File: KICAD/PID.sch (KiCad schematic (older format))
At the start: 4 parts, among them U3 Opamp_Dual_Generic

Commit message: removed legacy symbols
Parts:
- removed JP4, JP5: Jumper_NC_Small, symbol sesame-fonctionnel-rescue:Jumper_NC_Small-device
- removed U3: Opamp_Dual_Generic, symbol sesame-fonctionnel-rescue:Opamp_Dual_Generic-device
- added JP? (x2): Jumper_NO_Small, symbol Device:Jumper_NO_Small
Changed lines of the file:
@@
 $Descr A4 11693 8268
 encoding utf-8
-Sheet 12 15
+Sheet 10 15
 Title "SESAME"
 Date ""
@@
 Comment4 ""
 $EndDescr
-Text HLabel 3150 3150 0    50   Input ~ 0
+Text HLabel 3150 3250 0    50   Input ~ 0
 Selected_Measure
-Text Label 3300 3150 0    50   ~ 0
+Text Label 3300 3250 0    50   ~ 0
 Sel_Measure_In
-Text Label 4550 3150 0    50   ~ 0
+Text Label 4550 3250 0    50   ~ 0
 Sel_Measure_Ext
 Wire Wire Line
-	3150 3150 3900 3150
+	3150 3250 3900 3250
 Text HLabel 3150 2950 0    50   Input ~ 0
 Ext_Consign
@@
 Text Label 1200 1150 0    50   ~ 0
 Consign_Ext
-$Comp
-L sesame-fonctionnel-rescue:Jumper_NC_Small-device JP4
-U 1 1 61D0773B
-P 4000 2950
-AR Path="/61D0773B" Ref="JP4"  Part="1"
-AR Path="/60F1B237/61D0773B" Ref="JP4"  Part="1"
-F 0 "JP4" H 4000 3150 50  0000 C CNN
-F 1 "Jumper_NC_Small" H 4000 3071 50  0000 C CNN
-F 2 "" H 4000 2950 50  0001 C CNN
-F 3 "~" H 4000 2950 50  0001 C CNN
-	1    4000 2950
-	1    0    0    -1
-$EndComp
 Wire Wire Line
 	3150 2950 3900 2950
-$Comp
-L sesame-fonctionnel-rescue:Jumper_NC_Small-device JP5
-U 1 1 61D09C0A
-P 4000 3150
-AR Path="/61D09C0A" Ref="JP5"  Part="1"
-AR Path="/60F1B237/61D09C0A" Ref="JP5"  Part="1"
-F 0 "JP5" H 4000 2950 50  0000 C CNN
-F 1 "Jumper_NC_Small" H 4000 3050 50  0000 C CNN
-F 2 "" H 4000 3150 50  0001 C CNN
-F 3 "~" H 4000 3150 50  0001 C CNN
-	1    4000 3150
-	1    0    0    -1
-$EndComp
 Wire Wire Line
 	4100 2950 5250 2950
 Wire Wire Line
-	4100 3150 5250 3150
-$Comp
-L sesame-fonctionnel-rescue:Opamp_Dual_Generic-device U3
-U 1 1 61B777D2
-P 5550 3050
-AR Path="/61B777D2" Ref="U3"  Part="1"
-AR Path="/60F1B237/61B777D2" Ref="U3"  Part="1"
-F 0 "U3" H 5550 3417 50  0000 C CNN
-F 1 "Opamp_Dual_Generic" H 5550 3326 50  0000 C CNN
-F 2 "" H 5550 3050 50  0001 C CNN
-F 3 "~" H 5550 3050 50  0001 C CNN
-	1    5550 3050
-	1    0    0    -1
-$EndComp
+	4100 3250 5250 3250
 Wire Notes Line
 	600  2150 600  550
@@
 Wire Wire Line
 	1200 1250 1100 1250
+$Comp
+L Device:Jumper_NO_Small JP?
+U 1 1 610BA839
+P 4000 2950
+F 0 "JP?" H 4000 3135 50  0000 C CNN
+F 1 "Jumper_NO_Small" H 4000 3044 50  0000 C CNN
+F 2 "" H 4000 2950 50  0001 C CNN
+F 3 "~" H 4000 2950 50  0001 C CNN
+	1    4000 2950
+	1    0    0    -1
+$EndComp
+$Comp
+L Device:Jumper_NO_Small JP?
+U 1 1 610BB003
+P 4000 3250
+F 0 "JP?" H 4000 3435 50  0000 C CNN
+F 1 "Jumper_NO_Small" H 4000 3344 50  0000 C CNN
+F 2 "" H 4000 3250 50  0001 C CNN
+F 3 "~" H 4000 3250 50  0001 C CNN
+	1    4000 3250
+	1    0    0    -1
+$EndComp
 $EndSCHEMATC

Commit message: labels dans les blocks
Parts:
- removed JP? (x2): Jumper_NO_Small, symbol Device:Jumper_NO_Small
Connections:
- net labels added: Feedback, Measure_Selected
- net labels removed: Selected_Measure
- wire segments 16 -> 12
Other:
- note added: "Entrées"
- note added: "Sortie"
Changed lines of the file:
@@
 $Descr A4 11693 8268
 encoding utf-8
-Sheet 10 15
+Sheet 9 15
 Title "SESAME"
 Date ""
@@
 Comment4 ""
 $EndDescr
-Text HLabel 3150 3250 0    50   Input ~ 0
-Selected_Measure
-Text Label 3300 3250 0    50   ~ 0
-Sel_Measure_In
-Text Label 4550 3250 0    50   ~ 0
-Sel_Measure_Ext
-Wire Wire Line
-	3150 3250 3900 3250
-Text HLabel 3150 2950 0    50   Input ~ 0
+Text HLabel 5300 3550 0    50   Input ~ 0
+Measure_Selected
+Text HLabel 5300 3400 0    50   Input ~ 0
 Ext_Consign
-Text Label 3350 2950 0    50   ~ 0
-Consign_In
-Text Label 4550 2950 0    50   ~ 0
-Consign_Ext
 $Comp
 L Sesame:SESAME_SHIELD SLD1
@@
 Text Label 1200 1150 0    50   ~ 0
 Consign_Ext
-Wire Wire Line
-	3150 2950 3900 2950
-Wire Wire Line
-	4100 2950 5250 2950
-Wire Wire Line
-	4100 3250 5250 3250
 Wire Notes Line
 	600  2150 600  550
@@
 Wire Wire Line
 	1200 1250 1100 1250
-$Comp
-L Device:Jumper_NO_Small JP?
-U 1 1 610BA839
-P 4000 2950
-F 0 "JP?" H 4000 3135 50  0000 C CNN
-F 1 "Jumper_NO_Small" H 4000 3044 50  0000 C CNN
-F 2 "" H 4000 2950 50  0001 C CNN
-F 3 "~" H 4000 2950 50  0001 C CNN
-	1    4000 2950
-	1    0    0    -1
-$EndComp
-$Comp
-L Device:Jumper_NO_Small JP?
-U 1 1 610BB003
-P 4000 3250
-F 0 "JP?" H 4000 3435 50  0000 C CNN
-F 1 "Jumper_NO_Small" H 4000 3344 50  0000 C CNN
-F 2 "" H 4000 3250 50  0001 C CNN
-F 3 "~" H 4000 3250 50  0001 C CNN
-	1    4000 3250
-	1    0    0    -1
-$EndComp
+Text HLabel 5850 3450 2    50   Output ~ 0
+Feedback
+Text Notes 4850 3750 0    50   ~ 0
+Entrées
+Text Notes 5950 3650 0    50   ~ 0
+Sortie
+Wire Notes Line
+	6300 3350 6300 3700
+Wire Notes Line
+	6300 3700 5800 3700
+Wire Notes Line
+	5800 3700 5800 3350
+Wire Notes Line
+	5800 3350 6300 3350
+Wire Notes Line
+	5400 3300 4500 3300
+Wire Notes Line
+	4500 3300 4500 3800
+Wire Notes Line
+	4500 3800 5400 3800
+Wire Notes Line
+	5400 3800 5400 3300
 $EndSCHEMATC

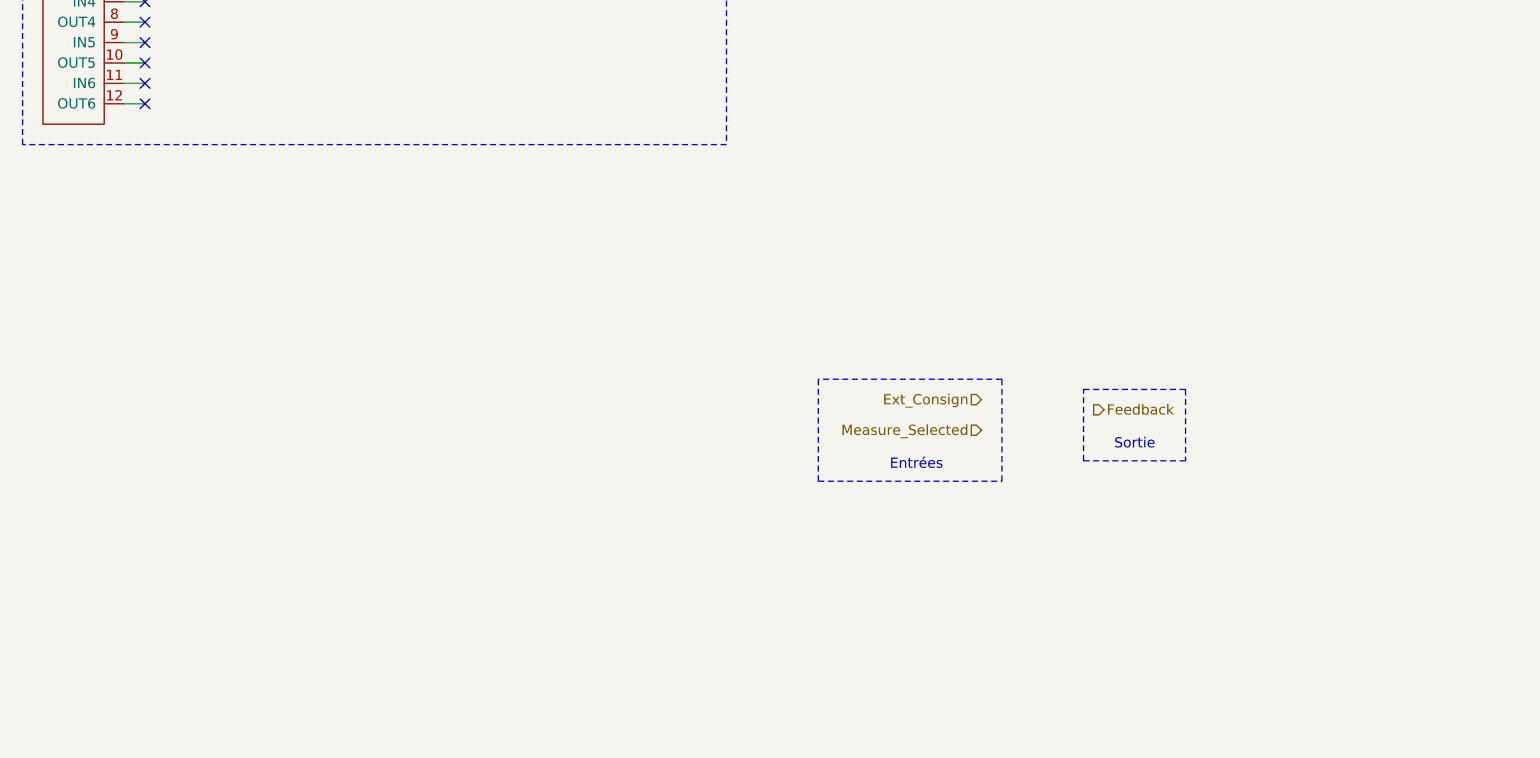
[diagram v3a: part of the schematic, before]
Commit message: added draft pwm gen & pid
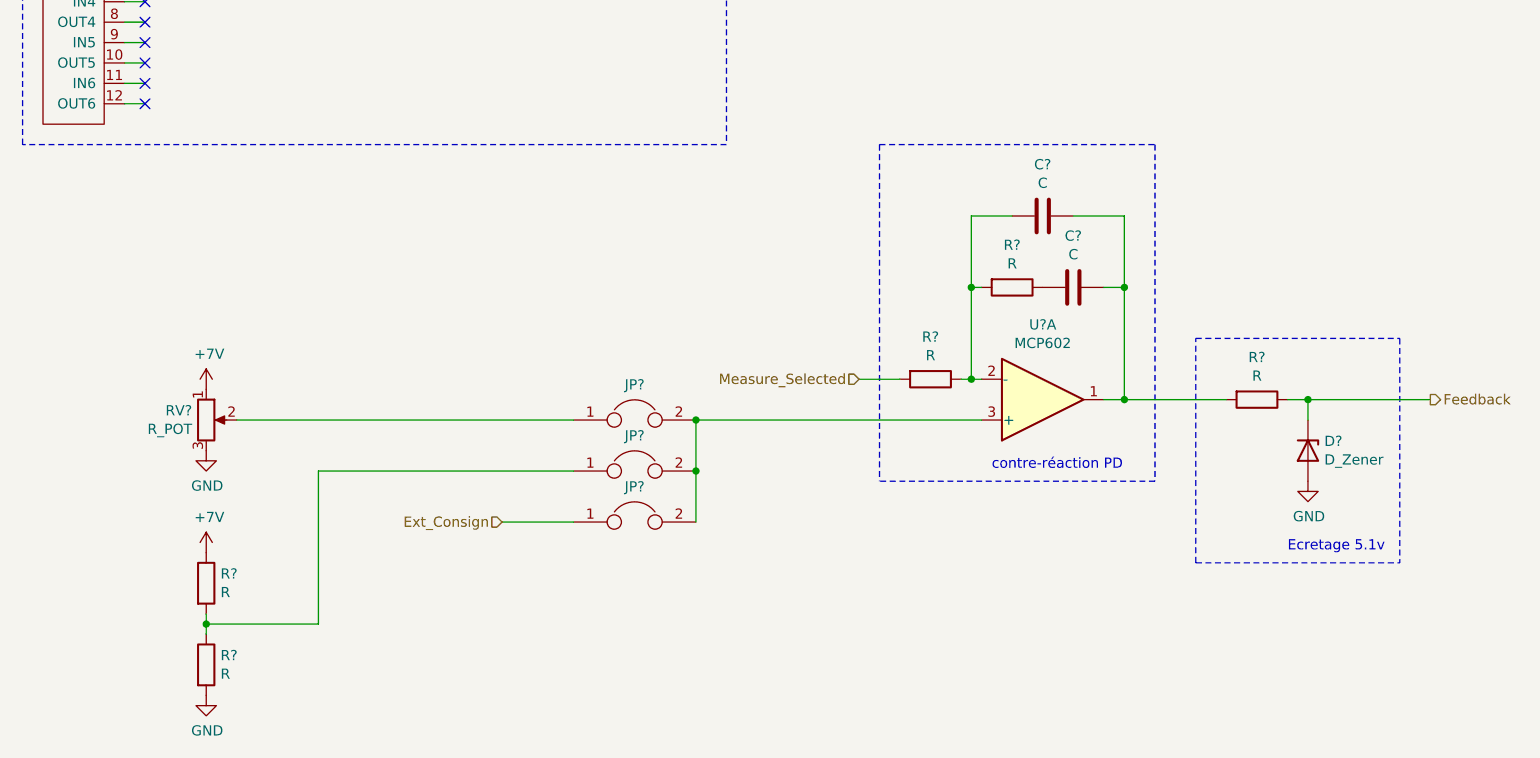
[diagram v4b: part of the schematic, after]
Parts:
- added C? (x2): C, symbol Device:C
- added D?: D_Zener, symbol Device:D_Zener
- added JP? (x3): Jumper, symbol Device:Jumper
- added R? (x5): R, symbol Device:R
- added RV?: R_POT, symbol Device:R_POT
- added U?: MCP602, symbol Amplifier_Operational:MCP602
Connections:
- net Ext_Consign: now also JP?.1
- net Feedback: now also D?.1 (K), R?.1
- net Measure_Selected: now also R?.2
- new net: C?.1, C?.1, R?.2, U?.1
- new net: C?.2, R?.1, R?.2, U?.2 (-)
- new net: JP?.2, JP?.2, JP?.2, U?.3 (+)
- new net: JP?.1, R?.1, R?.2
- new net: JP?.1, RV?.2
- new net: C?.2, R?.1
- new net +7V: R?.1, RV?.1
- new net GND: D?.2 (A), R?.2, RV?.3
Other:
- note added: "Ecretage 5.1v"
- note added: "contre-réaction PD"
- note removed: "Entrées"
- note removed: "Sortie"

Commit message: a ton of new stuff. V0.8
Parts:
- removed R? (x2): R, symbol Device:R
- removed RV?: R_POT, symbol Device:R_POT
- added C? (x2): C, symbol Device:C
- added C?: 100n, symbol Device:C
- added R? (x6): R, symbol Device:R
- added RV?: R_POT, symbol Device:R_POT
- added U?: LM7332, symbol Amplifier_Operational:LM7332
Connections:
- net Ext_Consign: now also R?.2; no longer JP?.1
- net GND: now also C?.2, C?.2, R?.2, RV?.3, U?.8 (V+)
- net Measure_Selected: now also R?.2
- net at C?.2, R?.1, R?.2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: now also C?.1
- net at JP?.2, JP?.2, JP?.2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: now also C?.1
- net at JP?.1: now also R?.1 (x2)
- new net: C?.2, R?.1
- new net: JP?.1, R?.1
- new net: R?.2, RV?.2
- new net: R?.1, R?.2, R?.2
- new net VCC: C?.1, U?.4 (V-)
- new net VREF: R?.1, RV?.1
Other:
- note added: "Alim. AOP"
- note added: "Consigne Fixe\nInterne"
- note added: "Consigne Potentiometre\nInterne"
- note added: "Soft start\nenv 1ms\nDemare apres le Enable (du driver)"
- note added: "contre-réaction PID"
- note removed: "contre-réaction PD"
- moved on the sheet: C?, D?, JP?, R?, U?A

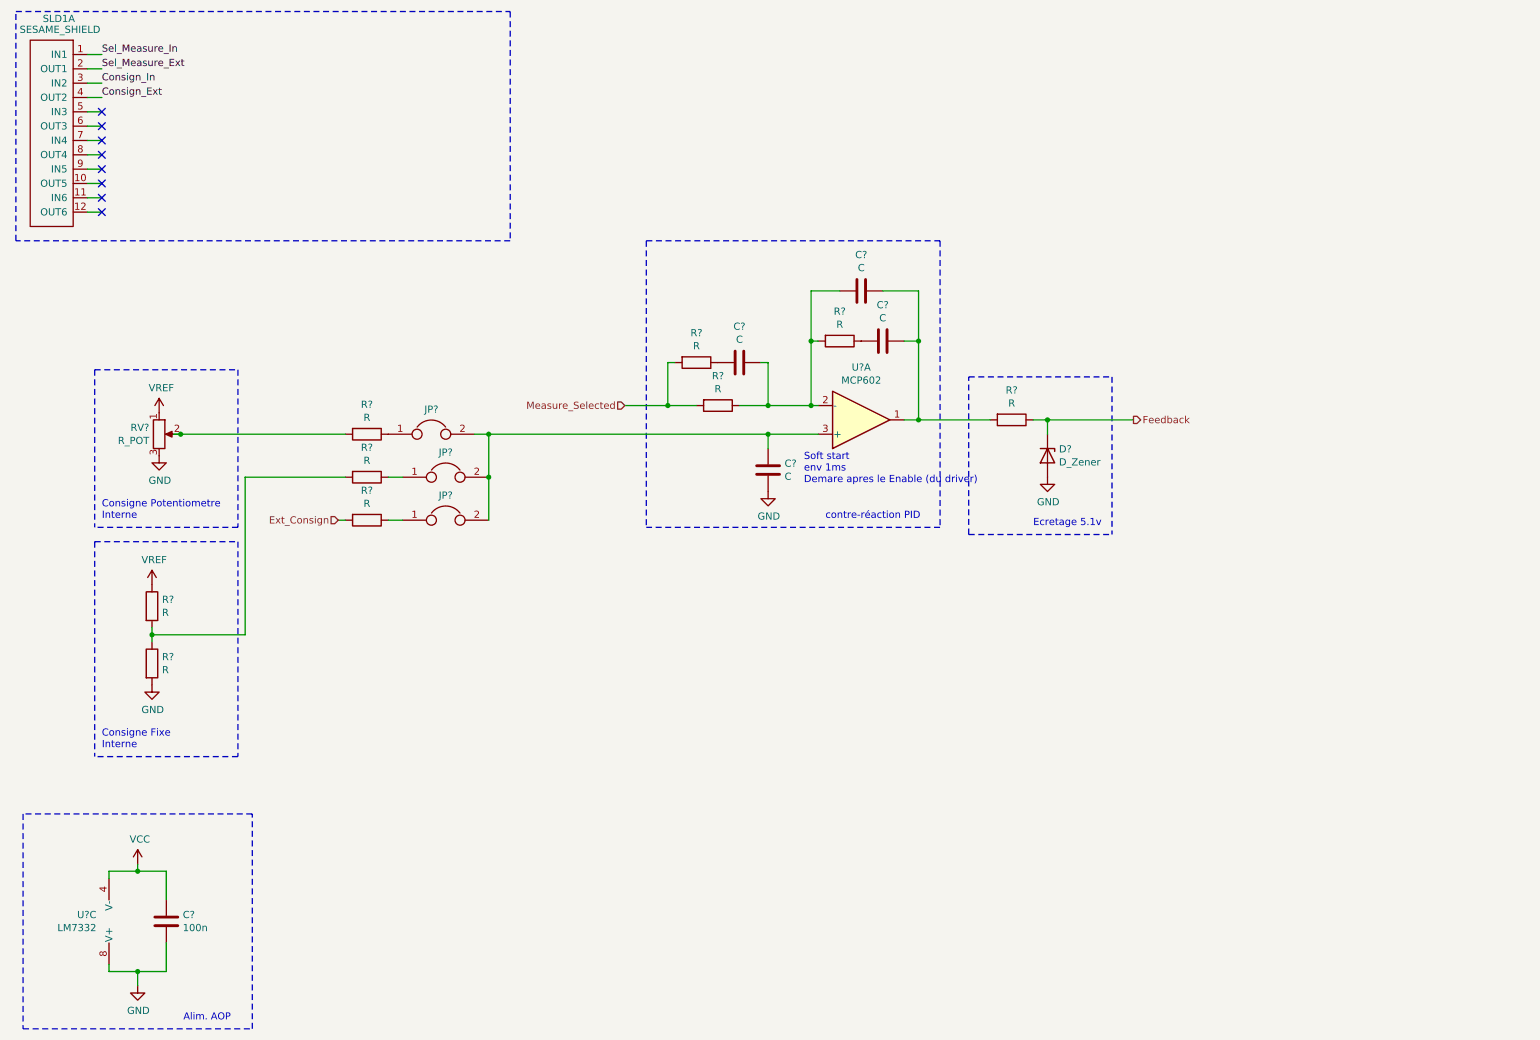
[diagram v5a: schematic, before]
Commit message: PID + PWM + RAMP finished
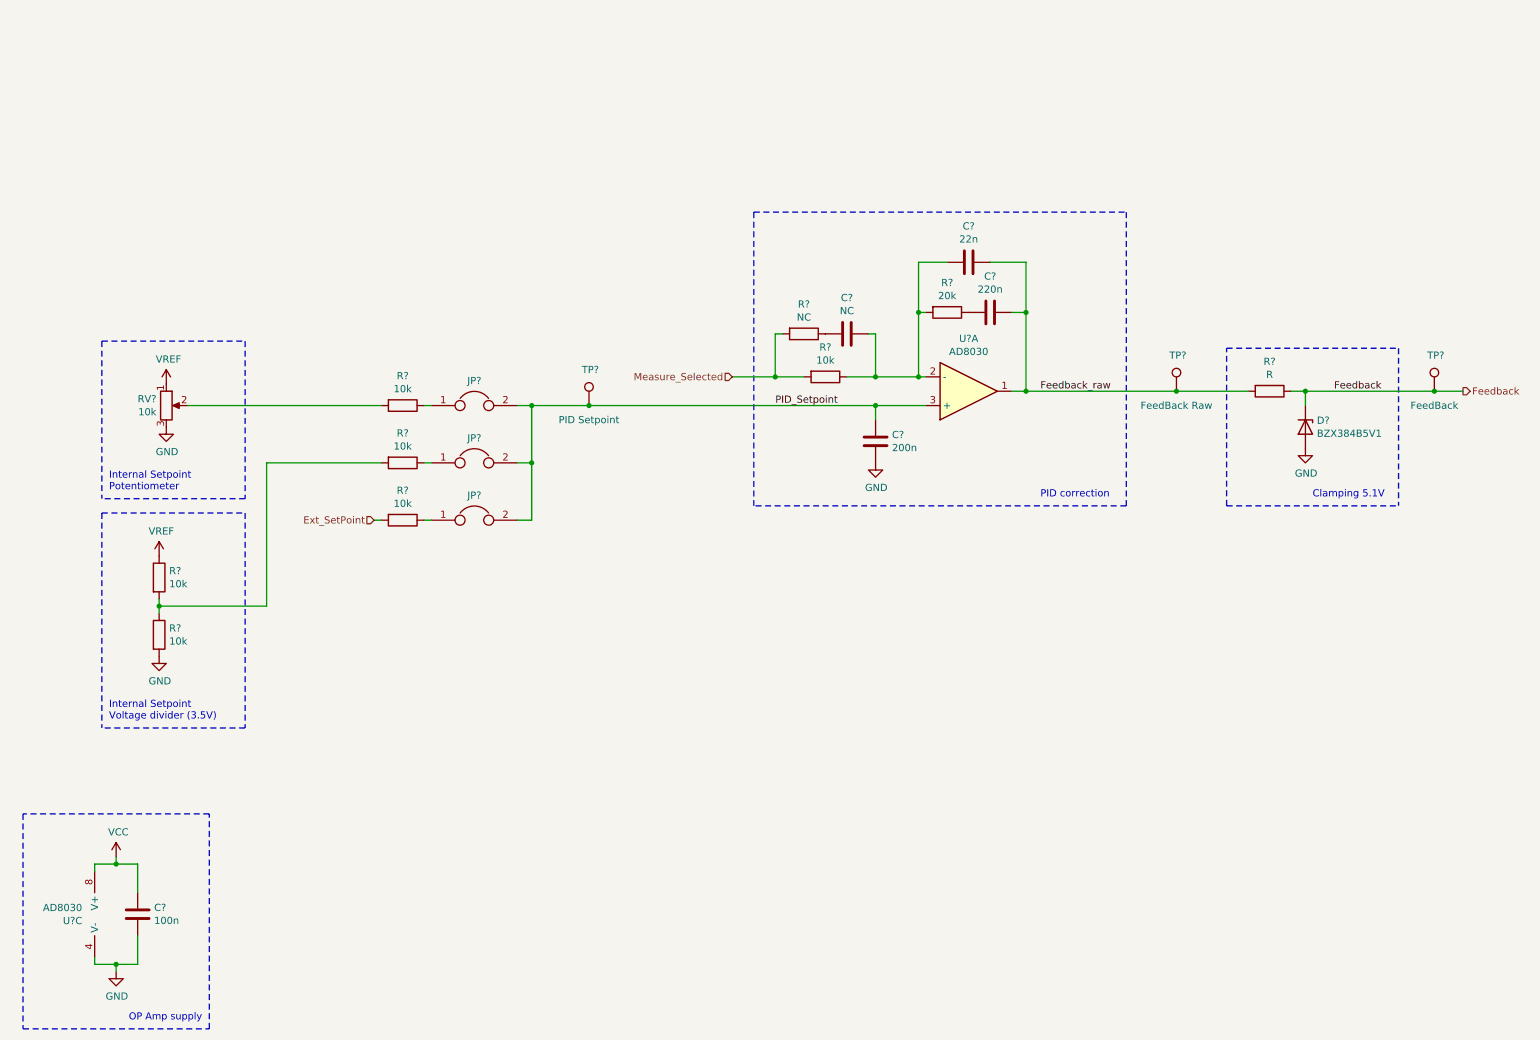
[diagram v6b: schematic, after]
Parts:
- removed C?: 100n, symbol Device:C
- removed JP?: Jumper, symbol Device:Jumper
- removed SLD1: SESAME_SHIELD, symbol Sesame:SESAME_SHIELD
- removed U?: LM7332, symbol Amplifier_Operational:LM7332
- removed U?: MCP602, symbol Amplifier_Operational:MCP602
- added C?: 100n, Capacitor_SMD:C_0805_2012Metric_Pad1.15x1.40mm_HandSolder, symbol Device:C
- added JP?: Jumper, symbol Device:Jumper
- added TP?: FeedBack Raw, symbol Connector:TestPoint
- added TP?: FeedBack, symbol Connector:TestPoint
- added TP?: PID Setpoint, symbol Connector:TestPoint
- added U? (x2): AD8030, symbol Sesame:AD8030
- C?: value C -> NC; footprint (none) -> Capacitor_SMD:C_0805_2012Metric_Pad1.15x1.40mm_HandSolder
- C?: value C -> 200n; footprint (none) -> Capacitor_SMD:C_0805_2012Metric_Pad1.15x1.40mm_HandSolder
- C?: value C -> 22n; footprint (none) -> Capacitor_SMD:C_0805_2012Metric_Pad1.15x1.40mm_HandSolder
- C?: value C -> 220n; footprint (none) -> Capacitor_SMD:C_0805_2012Metric_Pad1.15x1.40mm_HandSolder
- D?: value D_Zener -> BZX384B5V1; footprint (none) -> Diode_SMD:D_SOD-323_HandSoldering
- R?: value R -> NC; footprint (none) -> Resistor_SMD:R_0805_2012Metric_Pad1.15x1.40mm_HandSolder
- R? (x6): value R -> 10k; footprint (none) -> Resistor_SMD:R_0805_2012Metric_Pad1.15x1.40mm_HandSolder
- R?: value R -> 20k; footprint (none) -> Resistor_SMD:R_0805_2012Metric_Pad1.15x1.40mm_HandSolder
- R?: footprint (none) -> Resistor_SMD:R_0805_2012Metric_Pad1.15x1.40mm_HandSolder
- RV?: value R_POT -> 10k
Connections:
- net Feedback: now also TP?.1
- net GND: now also C?.2, U?.4 (V-)
- net VCC: now also C?.1, U?.8 (V+)
- net at C?.1, C?.2, R?.1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: now also U?.2 (-)
- net PID_Setpoint: now reaches C?.1, JP?.2, JP?.2
- net PID_Setpoint: now also JP?.2, TP?.1, U?.3 (+)
- net at R?.1: now also JP?.1
- net Feedback_raw: now reaches C?.1, C?.1, R?.2
- net Feedback_raw: now also TP?.1, U?.1
- net Ext_Consign renamed Ext_SetPoint
- no-connect marks 8 -> 0
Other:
- note added: "Clamping 5.1V"
- note added: "Internal Setpoint\nPotentiometer"
- note added: "Internal Setpoint\nVoltage divider (3.5V)"
- note added: "OP Amp supply"
- note added: "PID correction"
- note removed: "Alim. AOP"
- note removed: "Consigne Fixe\nInterne"
- note removed: "Consigne Potentiometre\nInterne"
- note removed: "Ecretage 5.1v"
- note removed: "Soft start\nenv 1ms\nDemare apres le Enable (du driver)"
- note removed: "contre-réaction PID"
- moved on the sheet: C?, D?, JP?, R?, RV?

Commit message: mainly footprints
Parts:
- U1: renamed from U?; footprint (none) -> Package_SO:SO-8_3.9x4.9mm_P1.27mm
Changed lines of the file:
@@
 $Descr A4 11693 8268
 encoding utf-8
-Sheet 8 16
+Sheet 4 16
 Title "SESAME"
 Date ""
@@
 P 1250 6850
 AR Path="/60F1AF26/6124BDFD" Ref="U?"  Part="3"
-AR Path="/60F1B237/6124BDFD" Ref="U?"  Part="3"
-F 0 "U?" H 1063 6804 50  0000 R CNN
+AR Path="/60F1B237/6124BDFD" Ref="U1"  Part="3"
+F 0 "U1" H 1063 6804 50  0000 R CNN
 F 1 "AD8030" H 1063 6895 50  0000 R CNN
-F 2 "" H 1250 6850 50  0001 C CNN
+F 2 "Package_SO:SO-8_3.9x4.9mm_P1.27mm" H 1250 6850 50  0001 C CNN
 F 3 "~" H 1250 6850 50  0001 C CNN
 	3    1250 6850
@@
 $EndComp
 $Comp
-L Sesame:AD8030 U?
+L Sesame:AD8030 U1
 U 1 1 6125EDE1
 P 7250 3200
-F 0 "U?" H 7250 2833 50  0000 C CNN
+F 0 "U1" H 7250 2833 50  0000 C CNN
 F 1 "AD8030" H 7250 2924 50  0000 C CNN
-F 2 "" H 7250 3200 50  0001 C CNN
+F 2 "Package_SO:SO-8_3.9x4.9mm_P1.27mm" H 7250 3200 50  0001 C CNN
 F 3 "~" H 7250 3200 50  0001 C CNN
 	1    7250 3200

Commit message: revex with jmt
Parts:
- TP?: value FeedBack Raw -> TP_NOP
- TP?: value FeedBack -> TP_POP
- TP?: value PID Setpoint -> TP_POP
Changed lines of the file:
@@
 $Descr A4 11693 8268
 encoding utf-8
-Sheet 4 16
+Sheet 3 16
 Title "SESAME"
 Date ""
@@
 AR Path="/60F1B237/612E229E" Ref="TP?"  Part="1"
 F 0 "TP?" H 8650 3450 50  0000 L CNN
-F 1 "FeedBack Raw" H 8700 3100 50  0000 C CNN
+F 1 "TP_NOP" H 8700 3100 50  0000 C CNN
 F 2 "" H 8900 3200 50  0001 C CNN
 F 3 "~" H 8900 3200 50  0001 C CNN
@@
 AR Path="/60F1B237/612E6FF3" Ref="TP?"  Part="1"
 F 0 "TP?" H 10450 3450 50  0000 L CNN
-F 1 "FeedBack" H 10500 3100 50  0000 C CNN
+F 1 "TP_POP" H 10500 3100 50  0000 C CNN
 F 2 "" H 10700 3200 50  0001 C CNN
 F 3 "~" H 10700 3200 50  0001 C CNN
@@
 AR Path="/60F1B237/612EF9C2" Ref="TP?"  Part="1"
 F 0 "TP?" H 4550 3550 50  0000 L CNN
-F 1 "PID Setpoint" H 4600 3200 50  0000 C CNN
+F 1 "TP_POP" H 4600 3200 50  0000 C CNN
 F 2 "" H 4800 3300 50  0001 C CNN
 F 3 "~" H 4800 3300 50  0001 C CNN
